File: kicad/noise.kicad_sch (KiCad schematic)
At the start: 9 parts, among them Q1 BC547, Q2 BC549C

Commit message: Changing decoupling caps to ceramic X7R
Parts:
- C1, C2: Spec ceramic C0G -> ceramic X7R
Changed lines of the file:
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@@
       (effects (font (size 1.27 1.27)) hide)
     )
-    (property "Spec" "ceramic C0G" (at 93.98 74.93 90)
+    (property "Spec" "ceramic X7R" (at 93.98 74.93 90)
       (effects (font (size 1.27 1.27)) hide)
     )
@@
       (effects (font (size 1.27 1.27)) hide)
     )
-    (property "Spec" "ceramic C0G" (at 123.19 68.58 90)
-      (effects (font (size 1.27 1.27)) hide)
-    )
+    (property "Spec" "ceramic X7R" (at 123.19 68.58 90)
+      (effects (font (size 1.27 1.27)) hide)
+    )

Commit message: Updating PCB and rebuilding ibom
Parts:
- Q1: value BC547 -> BC547C
- Q2: value BC549C -> BC547C
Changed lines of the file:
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@@
   (symbol (lib_id "Transistor_BJT:2N3904") (at 110.49 78.74 0) (unit 1)
     (in_bom yes) (on_board yes) (dnp no) (fields_autoplaced)
-    (property "Reference" "Q2" (at 115.3414 77.9053 0)
+    (property "Reference" "Q2" (at 115.57 78.105 0)
       (effects (font (size 1.27 1.27)) (justify left))
     )
-    (property "Value" "BC549C" (at 115.3414 80.4422 0)
+    (property "Value" "BC547C" (at 115.57 80.645 0)
       (effects (font (size 1.27 1.27)) (justify left))
     )
@@
       (effects (font (size 1.27 1.27)) (justify left))
     )
-    (property "Value" "BC547" (at 84.8614 88.0622 0)
+    (property "Value" "BC547C" (at 84.8614 88.0622 0)
       (effects (font (size 1.27 1.27)) (justify left))
     )

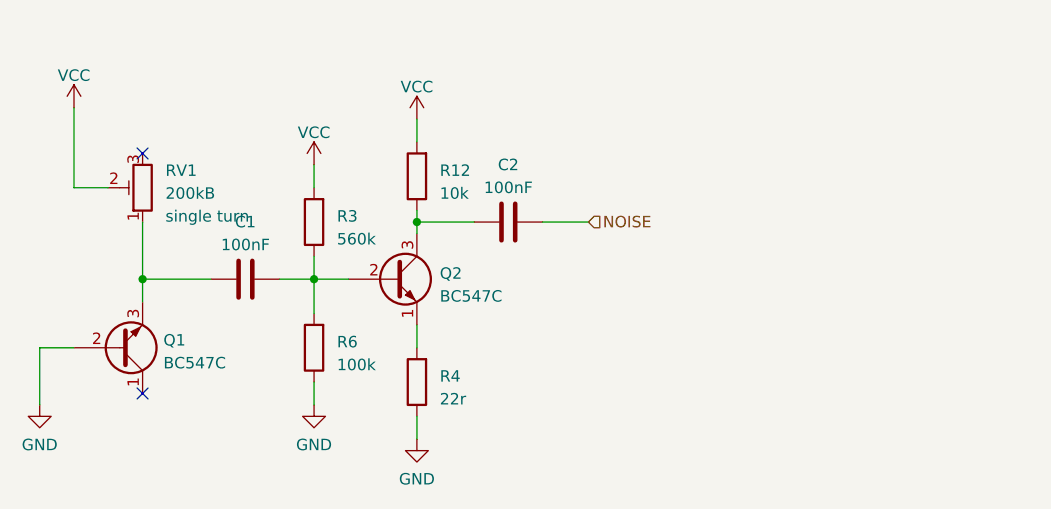
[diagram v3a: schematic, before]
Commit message: Updating board for new footprint libraries
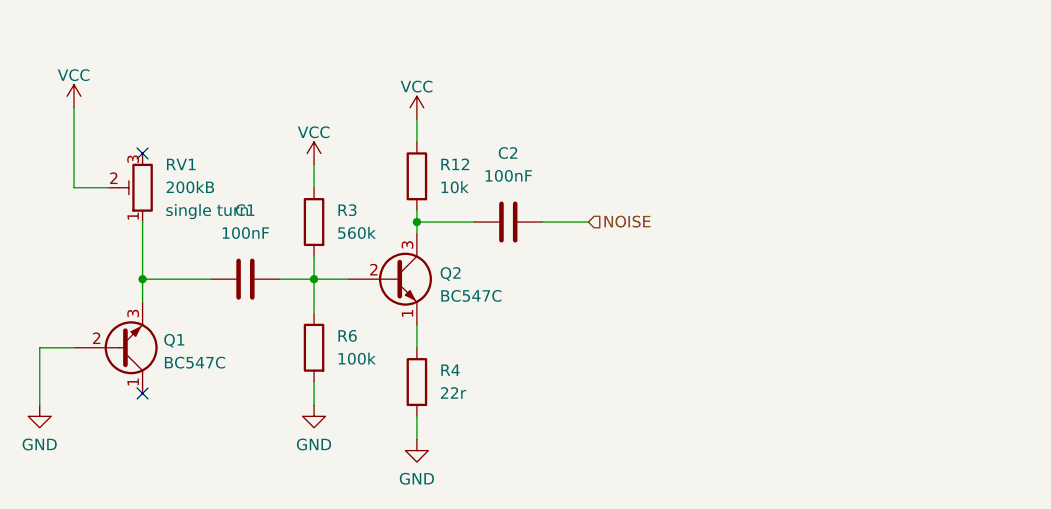
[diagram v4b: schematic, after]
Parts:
- C1, C2: symbol Rumblesan Standard Parts:C -> Rumblesan_Standard_Parts:C
- Q1, Q2: footprint Rumblesan_Standard_Parts:TO-92_Inline_Wide -> Package_TO_SOT_THT:TO-92_Inline_Wide
- R12, R3, R4, R6: symbol Rumblesan Standard Parts:R -> Rumblesan_Standard_Parts:R
- RV1: footprint Rumblesan_Standard_Parts:Potentiometer_THT_Bourns_3306P_Vertical -> Rumblesan_Potentiometer_THT:Potentiometer_THT_Bourns_3306P_Vertical; symbol Rumblesan Standard Parts:R_Potentiometer_Trim -> Rumblesan_Standard_Parts:R_Potentiometer_Trim
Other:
- moved on the sheet: R12, R3, R4, R6

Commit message: Tweaking noise circuitry
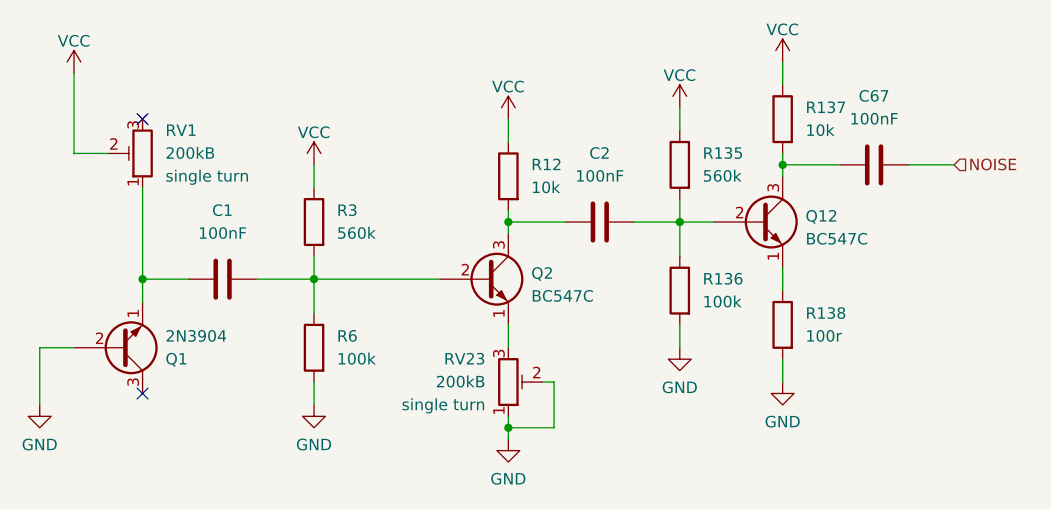
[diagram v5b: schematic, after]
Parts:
- removed Q1: BC547C, Package_TO_SOT_THT:TO-92_Inline_Wide, symbol Transistor_BJT:BC547
- removed R4: 22r, Rumblesan_Standard_Parts:R_Axial_DIN0207_L6.3mm_D2.5mm_P10.16mm_Horizontal, symbol Rumblesan_Standard_Parts:R
- added C67: 100nF, Rumblesan_Standard_Parts:C_Rect_L7.0mm_W2.5mm_P5.00mm, symbol Rumblesan_Standard_Parts:C
- added Q1: 2N3904, Package_TO_SOT_THT:TO-92_Inline_Wide, symbol Transistor_BJT:2N3904
- added Q12: BC547C, Package_TO_SOT_THT:TO-92_Inline_Wide, symbol Transistor_BJT:2N3904
- added R135: 560k, Rumblesan_Standard_Parts:R_Axial_DIN0207_L6.3mm_D2.5mm_P10.16mm_Horizontal, symbol Rumblesan_Standard_Parts:R
- added R136: 100k, Rumblesan_Standard_Parts:R_Axial_DIN0207_L6.3mm_D2.5mm_P10.16mm_Horizontal, symbol Rumblesan_Standard_Parts:R
- added R137: 10k, Rumblesan_Standard_Parts:R_Axial_DIN0207_L6.3mm_D2.5mm_P10.16mm_Horizontal, symbol Rumblesan_Standard_Parts:R
- added R138: 100r, Rumblesan_Standard_Parts:R_Axial_DIN0207_L6.3mm_D2.5mm_P10.16mm_Horizontal, symbol Rumblesan_Standard_Parts:R
- added RV23: 200kB, Rumblesan_Potentiometer_THT:Potentiometer_THT_Bourns_3306P_Vertical, symbol Rumblesan_Standard_Parts:R_Potentiometer_Trim
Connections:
- net GND: now also Q1.2 (B), R136.1, R138.1, RV23.1, RV23.2
- net NOISE: now also C67.2; no longer C2.2
- net VCC: now also R135.2, R137.2
- net at C1.1, RV1.1: now also Q1.1 (E)
- net at Q2.1 (E): now also RV23.3
- new net: Q12.1 (E), R138.2
- new net: C2.2, Q12.2 (B), R135.1, R136.2
- new net: C67.1, Q12.3 (C), R137.1
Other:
- moved on the sheet: C1, C2, Q2, R12, RV1

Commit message: Updating with rev03 changes
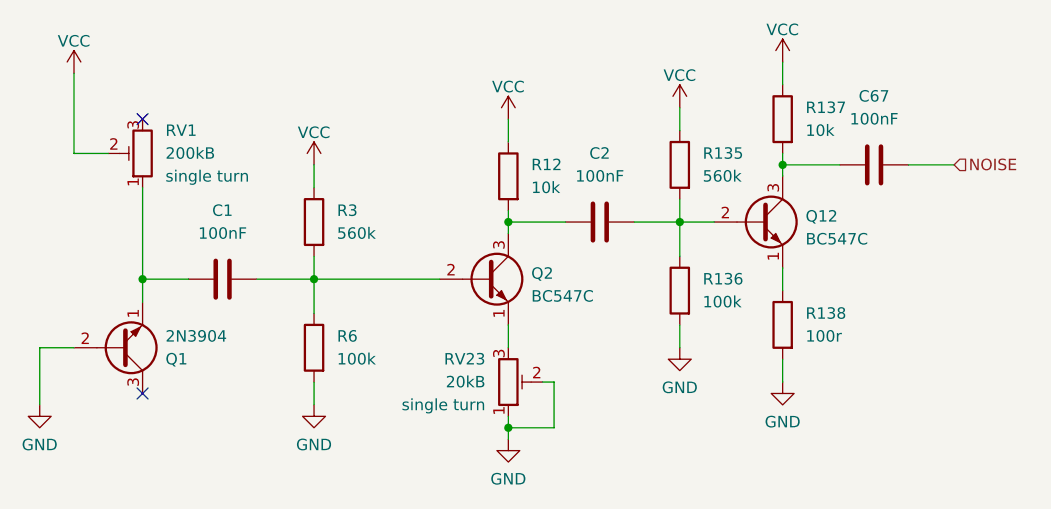
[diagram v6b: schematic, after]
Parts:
- RV1: footprint Rumblesan_Potentiometer_THT:Potentiometer_THT_Bourns_3306P_Vertical -> Rumblesan_Potentiometer_THT:Potentiometer_THT_Bourns_3306K
- RV23: value 200kB -> 20kB; footprint Rumblesan_Potentiometer_THT:Potentiometer_THT_Bourns_3306P_Vertical -> Rumblesan_Potentiometer_THT:Potentiometer_THT_Bourns_3306K
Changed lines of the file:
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@@
 (kicad_sch
-	(version 20231120)
+	(version 20250114)
 	(generator "eeschema")
-	(generator_version "8.0")
+	(generator_version "9.0")
 	(paper "A4")
 	(title_block
@@
 		(shape input)
 		(at 172.72 66.04 0)
-		(fields_autoplaced yes)
 		(effects
 			(font
@@
 			)
 		)
-		(property "Footprint" "Rumblesan_Potentiometer_THT:Potentiometer_THT_Bourns_3306P_Vertical"
+		(property "Footprint" "Rumblesan_Potentiometer_THT:Potentiometer_THT_Bourns_3306K"
 			(at 93.98 63.5 90)
 			(effects
@@
 			)
 		)
-		(property "Description" ""
+		(property "Description" "0.2A Ic, 40V Vce, Small Signal NPN Transistor, TO-92"
 			(at 151.13 72.39 0)
 			(effects
@@
 			)
 		)
-		(property "Description" ""
+		(property "Description" "0.2A Ic, 40V Vce, Small Signal NPN Transistor, TO-92"
 			(at 120.65 78.74 0)
 			(effects
@@
 			)
 		)
-		(property "Value" "200kB"
+		(property "Value" "20kB"
 			(at 120.65 90.1699 0)
 			(effects
@@
 			)
 		)
-		(property "Footprint" "Rumblesan_Potentiometer_THT:Potentiometer_THT_Bourns_3306P_Vertical"
+		(property "Footprint" "Rumblesan_Potentiometer_THT:Potentiometer_THT_Bourns_3306K"
 			(at 111.76 88.9 90)
 			(effects
